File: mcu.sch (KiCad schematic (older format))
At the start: 21 parts, among them SW1 SW_PUSH, U1 STM32F411RE_LQFP64, X1 32.768K, X2 8MHz

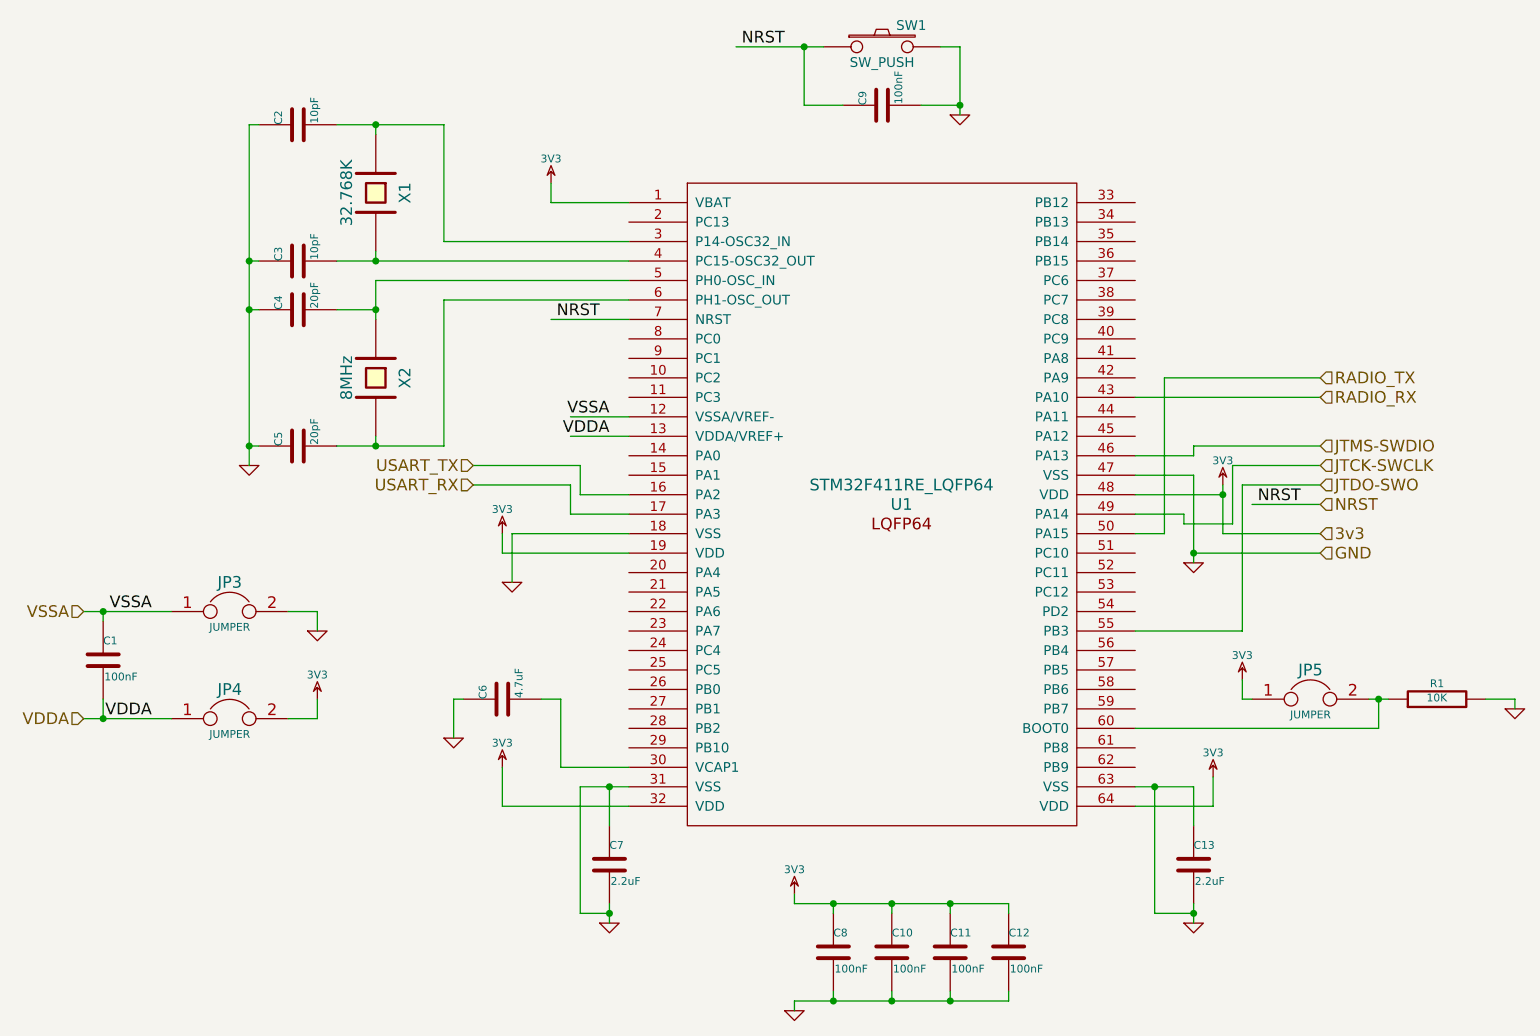
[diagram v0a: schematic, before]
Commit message: Added voltage regulators
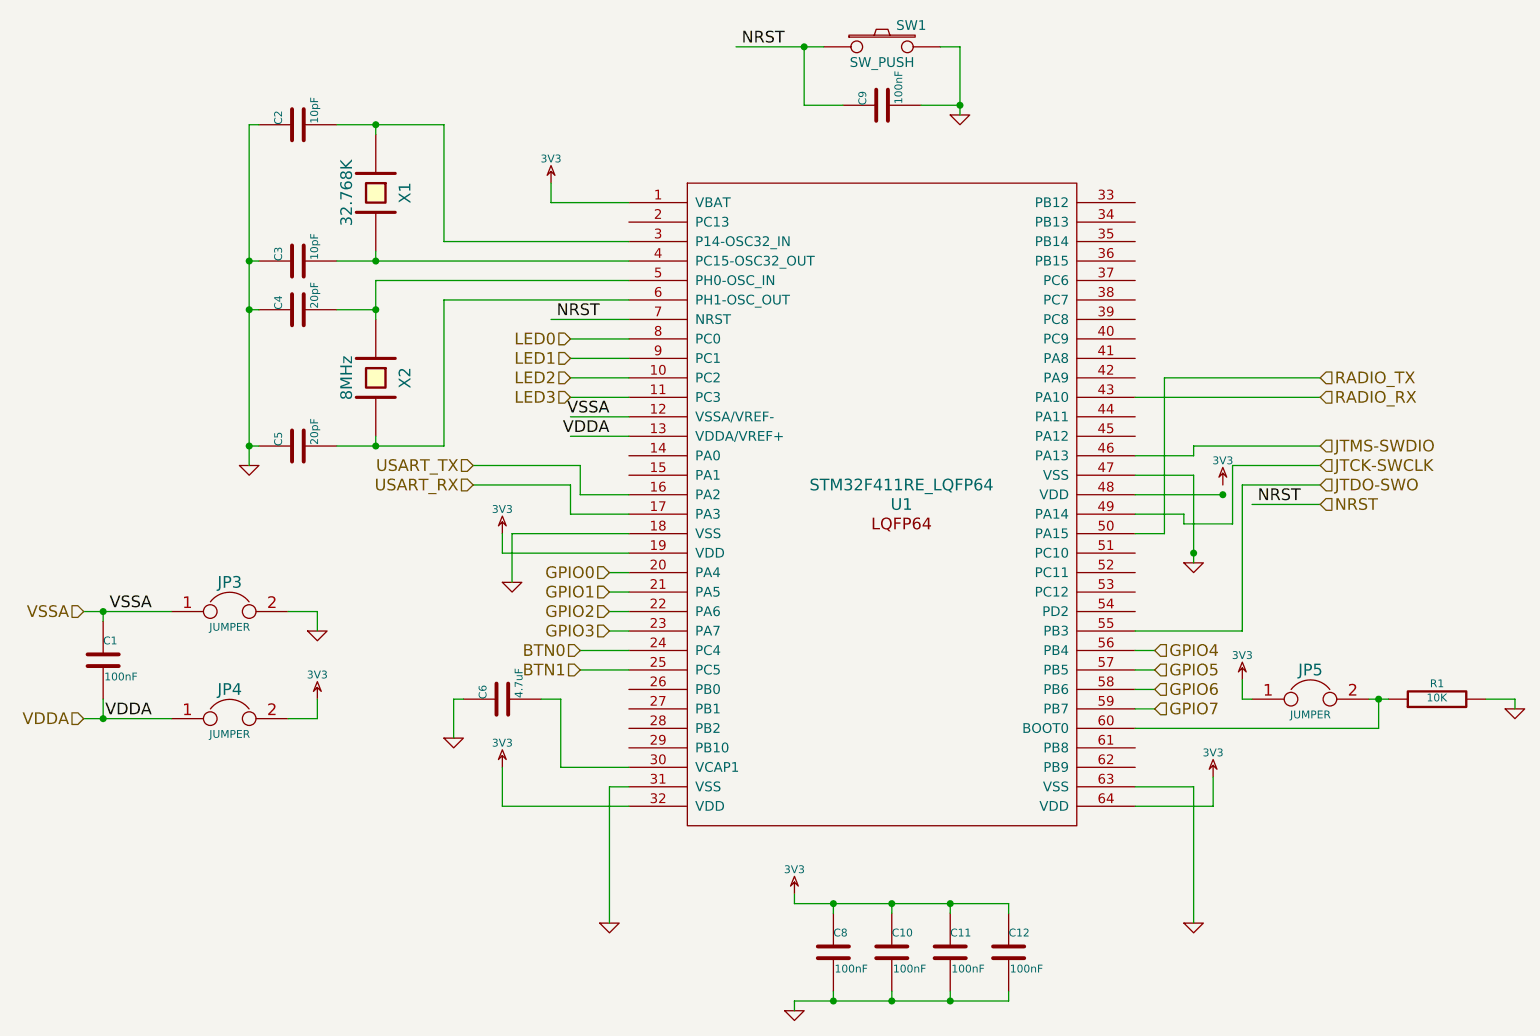
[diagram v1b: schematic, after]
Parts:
- removed C13, C7: 2.2uF, ~, symbol C
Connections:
- net labels added: BTN0, BTN1, GPIO0, GPIO1, GPIO2, GPIO3, GPIO4, GPIO5, GPIO6, GPIO7, LED0, LED1, LED2, LED3
- net labels removed: 3v3
- wire segments 107 -> 112

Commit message: Began layout of board
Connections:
- wire segments 112 -> 113
- no-connect marks 0 -> 25
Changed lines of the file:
@@
 LIBS:xbee
 LIBS:avbay-cache
-EELAYER 25 0
+EELAYER 27 0
 EELAYER END
 $Descr USLetter 11000 8500
@@
 Sheet 2 3
 Title "MCU"
-Date "5 oct 2014"
+Date "20 oct 2014"
 Rev ""
 Comp ""
@@
 $EndComp
 $Comp
-L 3V3 #PWR9
+L 3V3 #PWR010
 U 1 1 542CDA8F
 P 3800 3600
-F 0 "#PWR9" H 3800 3700 40  0001 C CNN
+F 0 "#PWR010" H 3800 3700 40  0001 C CNN
 F 1 "3V3" H 3800 3725 40  0000 C CNN
 F 2 "" H 3800 3600 60  0000 C CNN
@@
 $EndComp
 $Comp
-L GND #PWR11
+L GND #PWR011
 U 1 1 542CDA9E
 P 3850 3850
-F 0 "#PWR11" H 3850 3850 30  0001 C CNN
+F 0 "#PWR011" H 3850 3850 30  0001 C CNN
 F 1 "GND" H 3850 3780 30  0001 C CNN
 F 2 "" H 3850 3850 60  0000 C CNN
@@
 $EndComp
 $Comp
-L 3V3 #PWR10
+L 3V3 #PWR012
 U 1 1 542CDAB1
 P 3800 4800
-F 0 "#PWR10" H 3800 4900 40  0001 C CNN
+F 0 "#PWR012" H 3800 4900 40  0001 C CNN
 F 1 "3V3" H 3800 4925 40  0000 C CNN
 F 2 "" H 3800 4800 60  0000 C CNN
@@
 $EndComp
 $Comp
-L 3V3 #PWR19
+L 3V3 #PWR013
 U 1 1 542CDAB7
 P 7450 4850
-F 0 "#PWR19" H 7450 4950 40  0001 C CNN
+F 0 "#PWR013" H 7450 4950 40  0001 C CNN
 F 1 "3V3" H 7450 4975 40  0000 C CNN
 F 2 "" H 7450 4850 60  0000 C CNN
@@
 $EndComp
 $Comp
-L GND #PWR13
-U 1 1 542CDAC3
-P 4350 5600
-F 0 "#PWR13" H 4350 5600 30  0001 C CNN
-F 1 "GND" H 4350 5530 30  0001 C CNN
-F 2 "" H 4350 5600 60  0000 C CNN
-F 3 "" H 4350 5600 60  0000 C CNN
-	1    4350 5600
-	1    0    0    -1
-$EndComp
-$Comp
-L GND #PWR18
-U 1 1 542CDAC9
-P 7350 5600
-F 0 "#PWR18" H 7350 5600 30  0001 C CNN
-F 1 "GND" H 7350 5530 30  0001 C CNN
-F 2 "" H 7350 5600 60  0000 C CNN
-F 3 "" H 7350 5600 60  0000 C CNN
-	1    7350 5600
-	1    0    0    -1
-$EndComp
-$Comp
-L 3V3 #PWR20
+L 3V3 #PWR014
 U 1 1 542CDC4D
 P 7500 3350
-F 0 "#PWR20" H 7500 3450 40  0001 C CNN
+F 0 "#PWR014" H 7500 3450 40  0001 C CNN
 F 1 "3V3" H 7500 3475 40  0000 C CNN
 F 2 "" H 7500 3350 60  0000 C CNN
 F 3 "" H 7500 3350 60  0000 C CNN
 	1    7500 3350
-	1    0    0    -1
-$EndComp
-$Comp
-L GND #PWR17
-U 1 1 542CDC53
-P 7350 3750
-F 0 "#PWR17" H 7350 3750 30  0001 C CNN
-F 1 "GND" H 7350 3680 30  0001 C CNN
-F 2 "" H 7350 3750 60  0000 C CNN
-F 3 "" H 7350 3750 60  0000 C CNN
-	1    7350 3750
 	1    0    0    -1
 $EndComp
@@
 $EndComp
 $Comp
-L GND #PWR5
+L GND #PWR015
 U 1 1 5430D447
 P 2500 3250
-F 0 "#PWR5" H 2500 3250 30  0001 C CNN
+F 0 "#PWR015" H 2500 3250 30  0001 C CNN
 F 1 "GND" H 2500 3180 30  0001 C CNN
 F 2 "" H 2500 3250 60  0000 C CNN
@@
 $EndComp
 $Comp
-L GND #PWR16
+L GND #PWR016
 U 1 1 5430D873
 P 6150 1450
-F 0 "#PWR16" H 6150 1450 30  0001 C CNN
+F 0 "#PWR016" H 6150 1450 30  0001 C CNN
 F 1 "GND" H 6150 1380 30  0001 C CNN
 F 2 "" H 6150 1450 60  0000 C CNN
@@
 $EndComp
 $Comp
-L 3V3 #PWR21
+L 3V3 #PWR017
 U 1 1 5430DC01
 P 7600 4350
-F 0 "#PWR21" H 7600 4450 40  0001 C CNN
+F 0 "#PWR017" H 7600 4450 40  0001 C CNN
 F 1 "3V3" H 7600 4475 40  0000 C CNN
 F 2 "" H 7600 4350 60  0000 C CNN
@@
 $EndComp
 $Comp
-L GND #PWR22
+L GND #PWR018
 U 1 1 5430DC07
 P 9000 4500
-F 0 "#PWR22" H 9000 4500 30  0001 C CNN
+F 0 "#PWR018" H 9000 4500 30  0001 C CNN
 F 1 "GND" H 9000 4430 30  0001 C CNN
 F 2 "" H 9000 4500 60  0000 C CNN
@@
 $EndComp
 $Comp
-L 3V3 #PWR14
+L 3V3 #PWR019
 U 1 1 5430E0CC
 P 5300 5450
-F 0 "#PWR14" H 5300 5550 40  0001 C CNN
+F 0 "#PWR019" H 5300 5550 40  0001 C CNN
 F 1 "3V3" H 5300 5575 40  0000 C CNN
 F 2 "" H 5300 5450 60  0000 C CNN
@@
 $EndComp
 $Comp
-L GND #PWR15
+L GND #PWR020
 U 1 1 5430E365
 P 5300 6050
-F 0 "#PWR15" H 5300 6050 30  0001 C CNN
+F 0 "#PWR020" H 5300 6050 30  0001 C CNN
 F 1 "GND" H 5300 5980 30  0001 C CNN
 F 2 "" H 5300 6050 60  0000 C CNN
@@
 $EndComp
 $Comp
-L GND #PWR8
+L GND #PWR021
 U 1 1 5430E5BA
 P 3550 4650
-F 0 "#PWR8" H 3550 4650 30  0001 C CNN
+F 0 "#PWR021" H 3550 4650 30  0001 C CNN
 F 1 "GND" H 3550 4580 30  0001 C CNN
 F 2 "" H 3550 4650 60  0000 C CNN
@@
 VDDA
 $Comp
-L 3V3 #PWR12
+L 3V3 #PWR022
 U 1 1 5430E17B
 P 4050 1800
-F 0 "#PWR12" H 4050 1900 40  0001 C CNN
+F 0 "#PWR022" H 4050 1900 40  0001 C CNN
 F 1 "3V3" H 4050 1925 40  0000 C CNN
 F 2 "" H 4050 1800 60  0000 C CNN
@@
 VDDA
 $Comp
-L GND #PWR6
+L GND #PWR023
 U 1 1 5430E3DA
 P 2850 4100
-F 0 "#PWR6" H 2850 4100 30  0001 C CNN
+F 0 "#PWR023" H 2850 4100 30  0001 C CNN
 F 1 "GND" H 2850 4030 30  0001 C CNN
 F 2 "" H 2850 4100 60  0000 C CNN
@@
 $EndComp
 $Comp
-L 3V3 #PWR7
+L 3V3 #PWR024
 U 1 1 5430E3E0
 P 2850 4450
-F 0 "#PWR7" H 2850 4550 40  0001 C CNN
+F 0 "#PWR024" H 2850 4550 40  0001 C CNN
 F 1 "3V3" H 2850 4575 40  0000 C CNN
 F 2 "" H 2850 4450 60  0000 C CNN
@@
 	7050 3300 7350 3300
 Wire Wire Line
-	7350 3300 7350 3750
-Wire Wire Line
 	7050 3400 7500 3400
 Wire Wire Line
@@
 	4150 3350 3650 3350
 Connection ~ 7500 3400
-Connection ~ 7350 3700
 Wire Wire Line
 	2500 1500 2500 3250
@@
 	7050 4900 7350 4900
 Wire Wire Line
-	7350 4900 7350 5600
-Wire Wire Line
-	4450 4900 4350 4900
-Wire Wire Line
-	4350 4900 4350 5600
+	4150 4900 4450 4900
 Wire Wire Line
 	4450 2600 4150 2600
@@
 Text HLabel 7150 4500 2    60   Input ~ 0
 GPIO7
+NoConn ~ 7050 1900
+NoConn ~ 7050 2000
+NoConn ~ 7050 2100
+NoConn ~ 7050 2200
+NoConn ~ 7050 2300
+NoConn ~ 7050 2400
+NoConn ~ 7050 2500
+NoConn ~ 7050 2600
+NoConn ~ 7050 2700
+NoConn ~ 7050 2800
+NoConn ~ 7050 3000
+NoConn ~ 7050 3100
+NoConn ~ 7050 3700
+NoConn ~ 7050 3800
+NoConn ~ 7050 3900
+NoConn ~ 7050 4000
+NoConn ~ 7050 4700
+NoConn ~ 7050 4800
+NoConn ~ 4450 4700
+NoConn ~ 4450 4600
+NoConn ~ 4450 4500
+NoConn ~ 4450 4400
+NoConn ~ 4450 3300
+NoConn ~ 4450 3200
+NoConn ~ 4450 2000
+Wire Wire Line
+	7500 3400 7500 3350
+Wire Wire Line
+	4150 4900 4150 5300
+$Comp
+L GND #PWR025
+U 1 1 54449600
+P 4150 5300
+F 0 "#PWR025" H 4150 5300 30  0001 C CNN
+F 1 "GND" H 4150 5230 30  0001 C CNN
+F 2 "" H 4150 5300 60  0000 C CNN
+F 3 "" H 4150 5300 60  0000 C CNN
+	1    4150 5300
+	1    0    0    -1
+$EndComp
+Wire Wire Line
+	7350 4900 7350 5100
+$Comp
+L GND #PWR027
+U 1 1 5444A762
+P 7350 3600
+F 0 "#PWR027" H 7350 3600 30  0001 C CNN
+F 1 "GND" H 7350 3530 30  0001 C CNN
+F 2 "" H 7350 3600 60  0000 C CNN
+F 3 "" H 7350 3600 60  0000 C CNN
+	1    7350 3600
+	1    0    0    -1
+$EndComp
+Wire Wire Line
+	7350 3300 7350 3600
+$Comp
+L GND #PWR026
+U 1 1 54449656
+P 7350 5100
+F 0 "#PWR026" H 7350 5100 30  0001 C CNN
+F 1 "GND" H 7350 5030 30  0001 C CNN
+F 2 "" H 7350 5100 60  0000 C CNN
+F 3 "" H 7350 5100 60  0000 C CNN
+	1    7350 5100
+	1    0    0    -1
+$EndComp
 $EndSCHEMATC

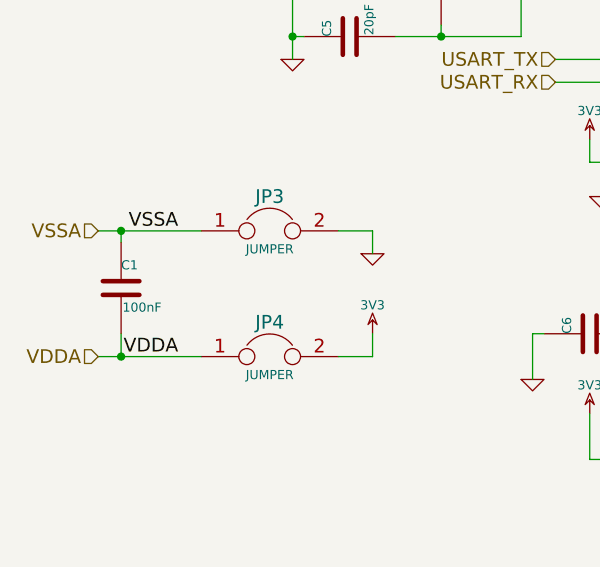
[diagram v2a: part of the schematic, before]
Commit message: Changed stuff
Layed out board with regulators, leds, and GPIOs
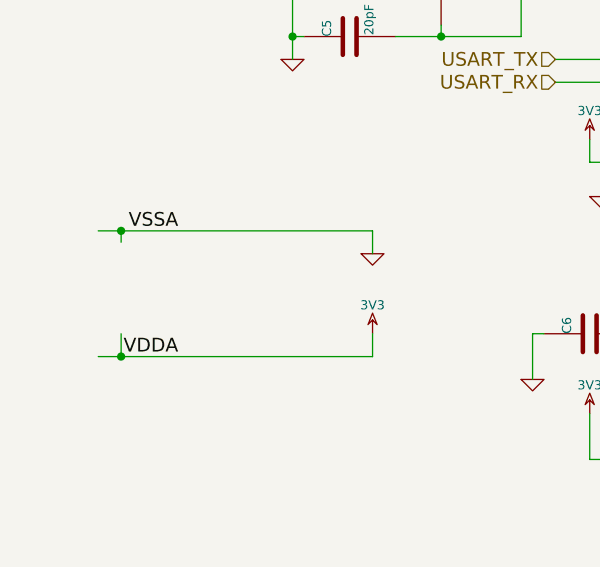
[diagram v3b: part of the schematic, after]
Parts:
- removed C1: 100nF, ~, symbol C
- removed JP3, JP4: JUMPER, ~, symbol JUMPER
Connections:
- wire segments 113 -> 111
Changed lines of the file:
@@
 $EndComp
 $Comp
-L 3V3 #PWR010
+L 3V3 #PWR08
 U 1 1 542CDA8F
 P 3800 3600
-F 0 "#PWR010" H 3800 3700 40  0001 C CNN
+F 0 "#PWR08" H 3800 3700 40  0001 C CNN
 F 1 "3V3" H 3800 3725 40  0000 C CNN
 F 2 "" H 3800 3600 60  0000 C CNN
@@
 $EndComp
 $Comp
-L GND #PWR011
+L GND #PWR09
 U 1 1 542CDA9E
 P 3850 3850
-F 0 "#PWR011" H 3850 3850 30  0001 C CNN
+F 0 "#PWR09" H 3850 3850 30  0001 C CNN
 F 1 "GND" H 3850 3780 30  0001 C CNN
 F 2 "" H 3850 3850 60  0000 C CNN
@@
 $EndComp
 $Comp
-L 3V3 #PWR012
+L 3V3 #PWR010
 U 1 1 542CDAB1
 P 3800 4800
-F 0 "#PWR012" H 3800 4900 40  0001 C CNN
+F 0 "#PWR010" H 3800 4900 40  0001 C CNN
 F 1 "3V3" H 3800 4925 40  0000 C CNN
 F 2 "" H 3800 4800 60  0000 C CNN
@@
 $EndComp
 $Comp
-L 3V3 #PWR013
+L 3V3 #PWR011
 U 1 1 542CDAB7
 P 7450 4850
-F 0 "#PWR013" H 7450 4950 40  0001 C CNN
+F 0 "#PWR011" H 7450 4950 40  0001 C CNN
 F 1 "3V3" H 7450 4975 40  0000 C CNN
 F 2 "" H 7450 4850 60  0000 C CNN
@@
 $EndComp
 $Comp
-L 3V3 #PWR014
+L 3V3 #PWR012
 U 1 1 542CDC4D
 P 7500 3350
-F 0 "#PWR014" H 7500 3450 40  0001 C CNN
+F 0 "#PWR012" H 7500 3450 40  0001 C CNN
 F 1 "3V3" H 7500 3475 40  0000 C CNN
 F 2 "" H 7500 3350 60  0000 C CNN
@@
 $EndComp
 $Comp
-L GND #PWR015
+L GND #PWR013
 U 1 1 5430D447
 P 2500 3250
-F 0 "#PWR015" H 2500 3250 30  0001 C CNN
+F 0 "#PWR013" H 2500 3250 30  0001 C CNN
 F 1 "GND" H 2500 3180 30  0001 C CNN
 F 2 "" H 2500 3250 60  0000 C CNN
@@
 $EndComp
 $Comp
-L GND #PWR016
+L GND #PWR014
 U 1 1 5430D873
 P 6150 1450
-F 0 "#PWR016" H 6150 1450 30  0001 C CNN
+F 0 "#PWR014" H 6150 1450 30  0001 C CNN
 F 1 "GND" H 6150 1380 30  0001 C CNN
 F 2 "" H 6150 1450 60  0000 C CNN
@@
 $EndComp
 $Comp
-L 3V3 #PWR017
+L 3V3 #PWR015
 U 1 1 5430DC01
 P 7600 4350
-F 0 "#PWR017" H 7600 4450 40  0001 C CNN
+F 0 "#PWR015" H 7600 4450 40  0001 C CNN
 F 1 "3V3" H 7600 4475 40  0000 C CNN
 F 2 "" H 7600 4350 60  0000 C CNN
@@
 $EndComp
 $Comp
-L GND #PWR018
+L GND #PWR016
 U 1 1 5430DC07
 P 9000 4500
-F 0 "#PWR018" H 9000 4500 30  0001 C CNN
+F 0 "#PWR016" H 9000 4500 30  0001 C CNN
 F 1 "GND" H 9000 4430 30  0001 C CNN
 F 2 "" H 9000 4500 60  0000 C CNN
@@
 $EndComp
 $Comp
-L 3V3 #PWR019
+L 3V3 #PWR017
 U 1 1 5430E0CC
 P 5300 5450
-F 0 "#PWR019" H 5300 5550 40  0001 C CNN
+F 0 "#PWR017" H 5300 5550 40  0001 C CNN
 F 1 "3V3" H 5300 5575 40  0000 C CNN
 F 2 "" H 5300 5450 60  0000 C CNN
@@
 $EndComp
 $Comp
-L GND #PWR020
+L GND #PWR018
 U 1 1 5430E365
 P 5300 6050
-F 0 "#PWR020" H 5300 6050 30  0001 C CNN
+F 0 "#PWR018" H 5300 6050 30  0001 C CNN
 F 1 "GND" H 5300 5980 30  0001 C CNN
 F 2 "" H 5300 6050 60  0000 C CNN
@@
 $EndComp
 $Comp
-L GND #PWR021
+L GND #PWR019
 U 1 1 5430E5BA
 P 3550 4650
-F 0 "#PWR021" H 3550 4650 30  0001 C CNN
+F 0 "#PWR019" H 3550 4650 30  0001 C CNN
 F 1 "GND" H 3550 4580 30  0001 C CNN
 F 2 "" H 3550 4650 60  0000 C CNN
@@
 VDDA
 $Comp
-L 3V3 #PWR022
+L 3V3 #PWR020
 U 1 1 5430E17B
 P 4050 1800
-F 0 "#PWR022" H 4050 1900 40  0001 C CNN
+F 0 "#PWR020" H 4050 1900 40  0001 C CNN
 F 1 "3V3" H 4050 1925 40  0000 C CNN
 F 2 "" H 4050 1800 60  0000 C CNN
@@
 $EndComp
 $Comp
-L JUMPER JP3
-U 1 1 5430E1F5
-P 2400 4000
-F 0 "JP3" H 2400 4150 60  0000 C CNN
-F 1 "JUMPER" H 2400 3920 40  0000 C CNN
-F 2 "~" H 2400 4000 60  0000 C CNN
-F 3 "~" H 2400 4000 60  0000 C CNN
-	1    2400 4000
-	1    0    0    -1
-$EndComp
-$Comp
-L JUMPER JP4
-U 1 1 5430E27E
-P 2400 4550
-F 0 "JP4" H 2400 4700 60  0000 C CNN
-F 1 "JUMPER" H 2400 4470 40  0000 C CNN
-F 2 "~" H 2400 4550 60  0000 C CNN
-F 3 "~" H 2400 4550 60  0000 C CNN
-	1    2400 4550
-	1    0    0    -1
-$EndComp
-Text HLabel 1650 4000 0    60   Input ~ 0
-VSSA
-Text HLabel 1650 4550 0    60   Input ~ 0
-VDDA
-$Comp
-L GND #PWR023
+L GND #PWR021
 U 1 1 5430E3DA
 P 2850 4100
-F 0 "#PWR023" H 2850 4100 30  0001 C CNN
+F 0 "#PWR021" H 2850 4100 30  0001 C CNN
 F 1 "GND" H 2850 4030 30  0001 C CNN
 F 2 "" H 2850 4100 60  0000 C CNN
@@
 $EndComp
 $Comp
-L 3V3 #PWR024
+L 3V3 #PWR022
 U 1 1 5430E3E0
 P 2850 4450
-F 0 "#PWR024" H 2850 4550 40  0001 C CNN
+F 0 "#PWR022" H 2850 4550 40  0001 C CNN
 F 1 "3V3" H 2850 4575 40  0000 C CNN
 F 2 "" H 2850 4450 60  0000 C CNN
 F 3 "" H 2850 4450 60  0000 C CNN
 	1    2850 4450
-	1    0    0    -1
-$EndComp
-$Comp
-L C C1
-U 1 1 5430EA07
-P 1750 4250
-F 0 "C1" H 1750 4350 40  0000 L CNN
-F 1 "100nF" H 1756 4165 40  0000 L CNN
-F 2 "~" H 1788 4100 30  0000 C CNN
-F 3 "~" H 1750 4250 60  0000 C CNN
-	1    1750 4250
 	1    0    0    -1
 $EndComp
@@
 	7200 2800 8000 2800
 Wire Wire Line
-	1650 4000 2100 4000
-Wire Wire Line
-	1650 4550 2100 4550
+	1650 4000 2850 4000
+Wire Wire Line
+	1650 4550 2850 4550
 Wire Wire Line
 	4050 1900 4450 1900
@@
 	4050 1800 4050 1900
 Wire Wire Line
-	2850 4100 2850 4000
-Wire Wire Line
-	2850 4000 2700 4000
-Wire Wire Line
-	2850 4450 2850 4550
-Wire Wire Line
-	2850 4550 2700 4550
+	2850 4000 2850 4100
+Wire Wire Line
+	2850 4550 2850 4450
 Wire Wire Line
 	1750 4450 1750 4550
@@
 	4150 4900 4150 5300
 $Comp
-L GND #PWR025
+L GND #PWR023
 U 1 1 54449600
 P 4150 5300
-F 0 "#PWR025" H 4150 5300 30  0001 C CNN
+F 0 "#PWR023" H 4150 5300 30  0001 C CNN
 F 1 "GND" H 4150 5230 30  0001 C CNN
 F 2 "" H 4150 5300 60  0000 C CNN
@@
 	7350 4900 7350 5100
 $Comp
-L GND #PWR027
+L GND #PWR024
 U 1 1 5444A762
 P 7350 3600
-F 0 "#PWR027" H 7350 3600 30  0001 C CNN
+F 0 "#PWR024" H 7350 3600 30  0001 C CNN
 F 1 "GND" H 7350 3530 30  0001 C CNN
 F 2 "" H 7350 3600 60  0000 C CNN
@@
 	7350 3300 7350 3600
 $Comp
-L GND #PWR026
+L GND #PWR025
 U 1 1 54449656
 P 7350 5100
-F 0 "#PWR026" H 7350 5100 30  0001 C CNN
+F 0 "#PWR025" H 7350 5100 30  0001 C CNN
 F 1 "GND" H 7350 5030 30  0001 C CNN
 F 2 "" H 7350 5100 60  0000 C CNN

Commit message: Made breakout board
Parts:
- removed JP5: JUMPER, ~, symbol JUMPER
- removed R1: 10K, ~, symbol R
- added P4, P5, P6, P7: CONN_01X16, Pin_Headers:Pin_Header_Straight_1x16, symbol CONN_01X16
- C10, C11, C12, C2, C3, C4, C5, C6, C8, C9: footprint ~ -> SMD_Packages:SMD-0805
- SW1: footprint ~ -> Discret:SW_PUSH_SMALL
- U1: footprint (none) -> Housings_QFP:LQFP-64_10x10mm_Pitch0.5mm
- X1, X2: footprint ~ -> Discret:HC-49V
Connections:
- net labels added: PA0, PA1, PA11, PA12, PA15, PA4, PA5, PA6, PA7, PA8, PA9, PB0, PB1, PB10, PB12, PB13, PB14, PB15, PB2, PB4, PB5, PB6, PB7, PB8, PB9, PC0, PC1, PC10, PC11, PC12, PC13, PC2, PC3, PC4, PC5, PC6, PC7, PC8, PC9, PD2
- net labels removed: BTN0, BTN1, GPIO0, GPIO1, GPIO2, GPIO3, GPIO4, GPIO5, GPIO6, GPIO7, LED0, LED1, LED2, LED3
- wire segments 111 -> 169
- no-connect marks 25 -> 0
